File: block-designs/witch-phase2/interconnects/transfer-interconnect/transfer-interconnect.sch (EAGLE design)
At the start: 60 parts, among them IC1 74LVC1G17DBV, IC10 74LVC1G17DBV, IC11 74LVC1G17DBV, IC12 74LVC1G17DBV, IC2 74LVC1G17DBV, IC3 74LVC1G17DBV, IC4 74LVC1G17DBV, IC5 74LVC1G17DBV, IC6 74LVC1G17DBV, IC7 74LVC1G17DBV, IC8 74LVC1G17DBV, IC9 74LVC1G17DBV

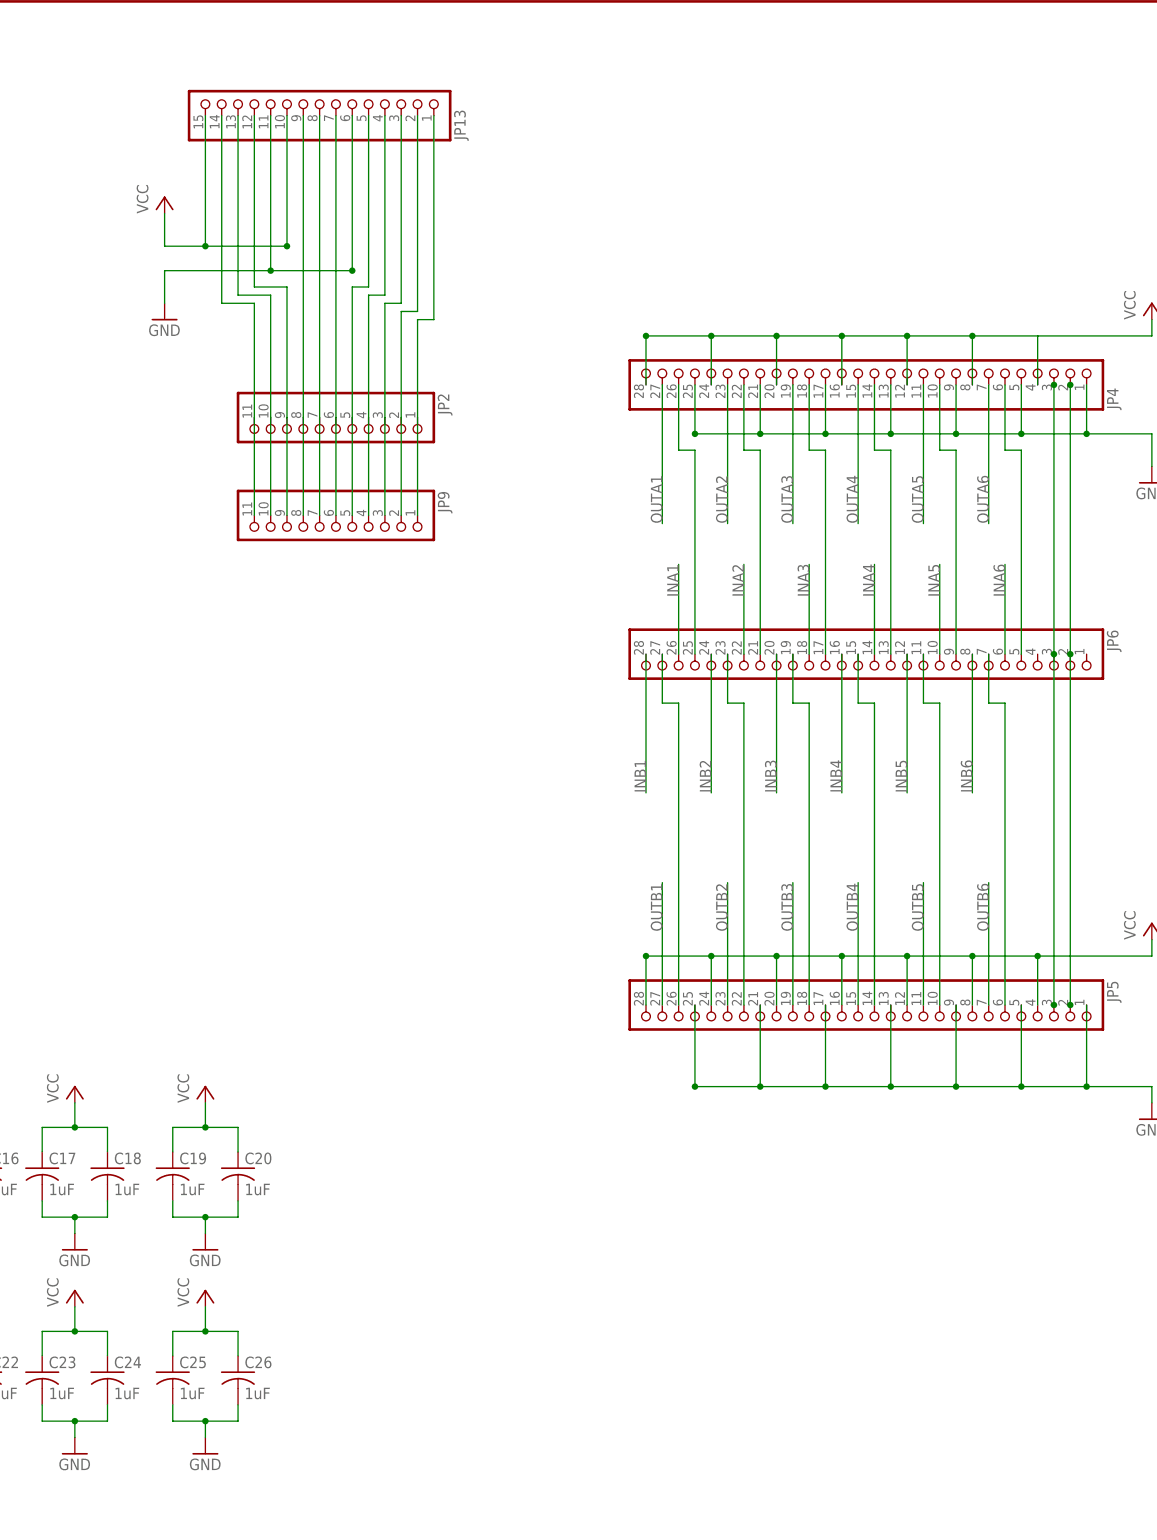
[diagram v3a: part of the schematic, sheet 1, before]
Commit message: add schmitt trigger on the carry output line
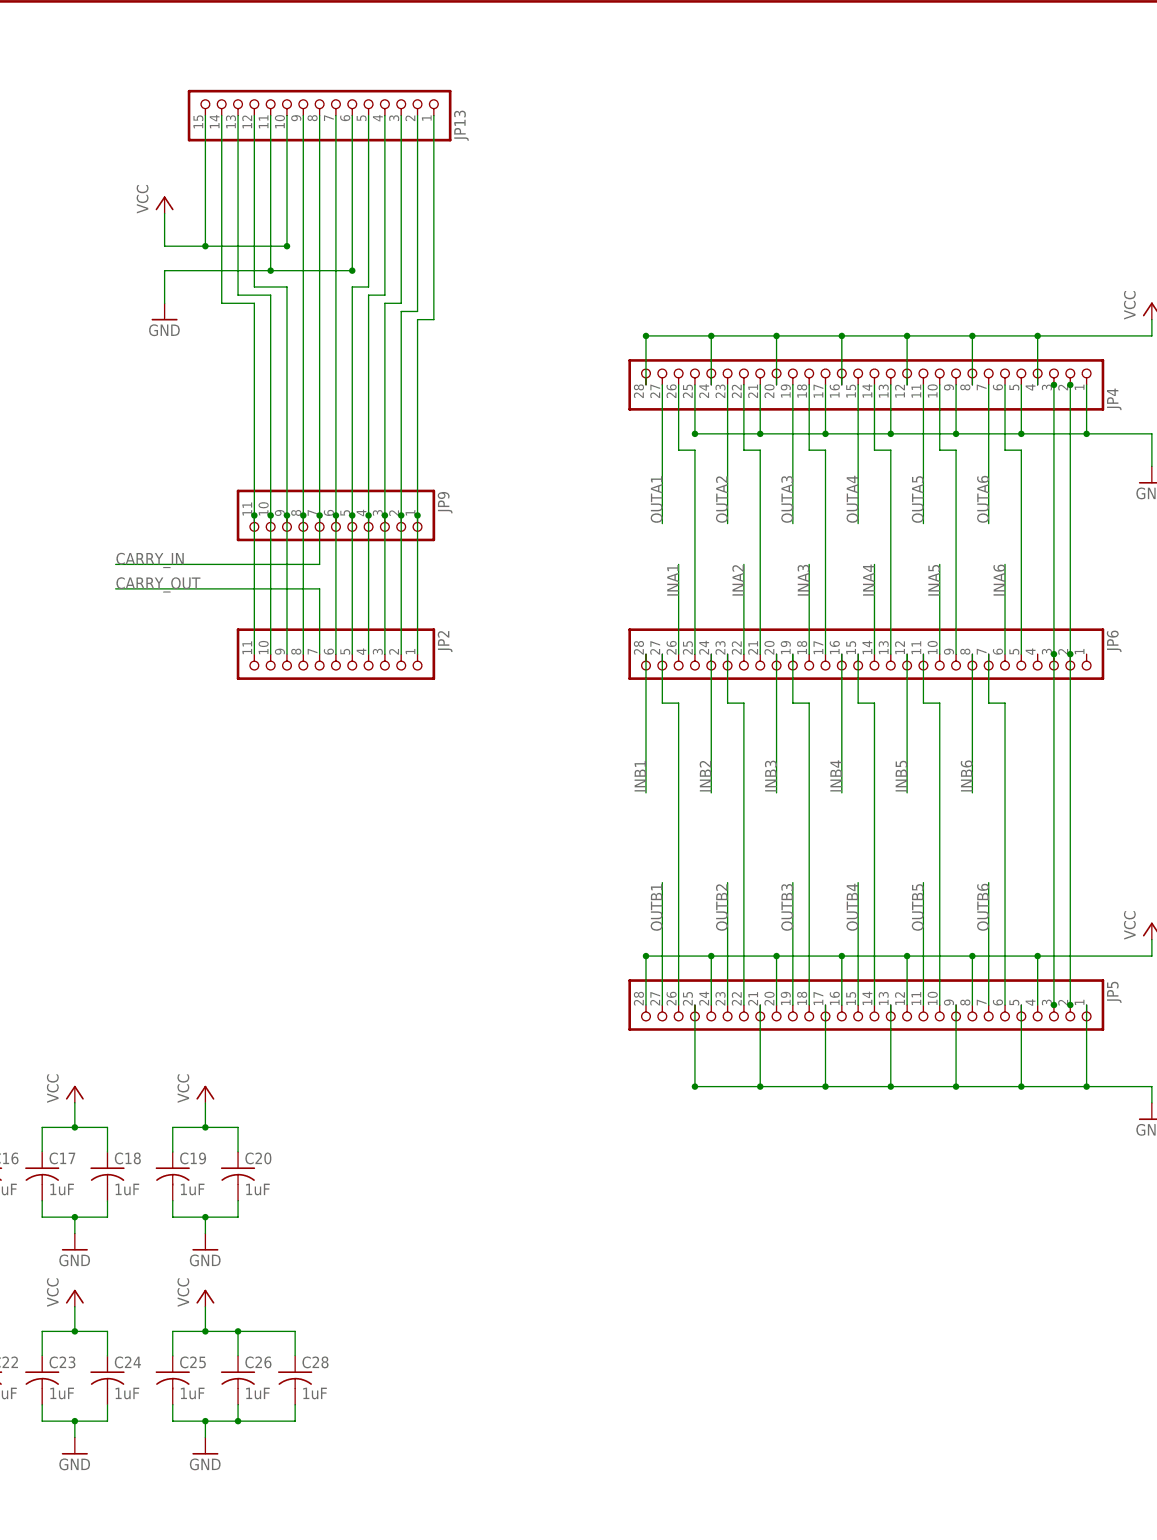
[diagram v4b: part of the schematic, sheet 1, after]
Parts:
- added C27, C28: 1uF, resistor:C-USC0603K
- added IC13: 74LVC1G17DBV, 74xx-little-us:74LVC1G17DBV
- added R13: 100k, resistor:R-US_R0603
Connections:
- removed net IN5: C8.1, IC6A.I, R6.1
- removed net IN6: C9.1, IC7A.I, R7.1
- removed net N$36: JP13.8, JP2.7, JP9.7
- new net CARRY_IN: C27.1, IC13A.I, JP13.8, JP9.7, R13.1
- new net CARRY_OUT: IC13A.O, JP2.7
- net GND: now also C27.2, C28.2
- net INA5: now also C8.1, IC6A.I, R6.1
- net INA6: now also C9.1, IC7A.I, R7.1
- net VCC: now also C28.1, R13.2
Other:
- moved on the sheet: JP2
